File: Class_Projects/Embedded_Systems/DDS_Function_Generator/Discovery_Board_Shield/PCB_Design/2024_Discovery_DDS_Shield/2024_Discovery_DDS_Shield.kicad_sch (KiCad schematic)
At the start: 66 parts, among them J1 FILTER_CONN, J2 10118194-0001LF, J3 FTDI_UART_CONN, J4 DC_OFFSET_CONN, J5 LCD_CONN, J6 Conn_OpAmp_Power, J7 Conn_DiscBoard_Right, J8 Conn_DiscBoard_Left, J9 BNC_CONN, SW2 SW_MODE, SW3 SW_CURSOR, SW4 SW_PLUS, SW5 SW_MINUS, SW6 SW_RUN_STOP, U1 TL072, U2 TL072, U5 FT230XS

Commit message: new board version
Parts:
- removed J3: FTDI_UART_CONN, Connector_PinHeader_2.54mm:PinHeader_1x03_P2.54mm_Vertical, symbol Connector_Generic:Conn_01x03
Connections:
- net GND: no longer D3.1 (K), D4.1 (K)
- net MODE: now also R7.2, R8.2
- net at U5.14 (CBUS1): now also D3.1 (K); no longer R7.2
- net at U5.7 (CBUS2): now also D4.1 (K); no longer R8.2
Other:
- moved on the sheet: C17, C18, D3, D4, J2, R10, R7, R8, R9, SW2, SW3, SW4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

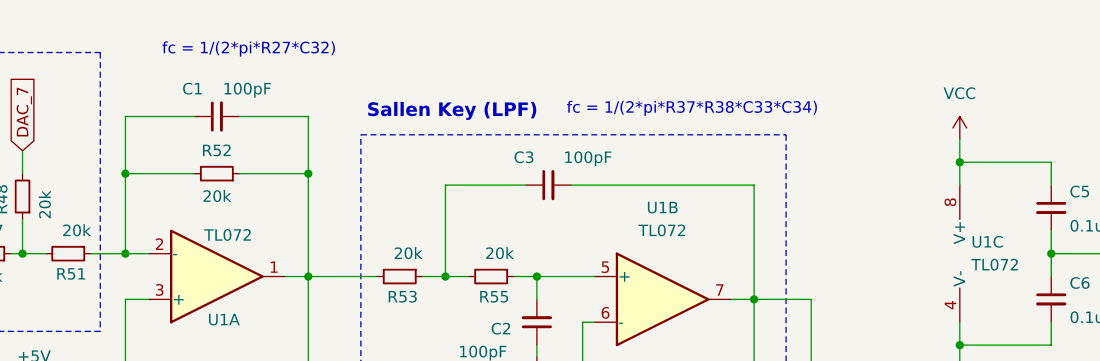
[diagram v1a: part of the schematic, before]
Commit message: schematics fixed
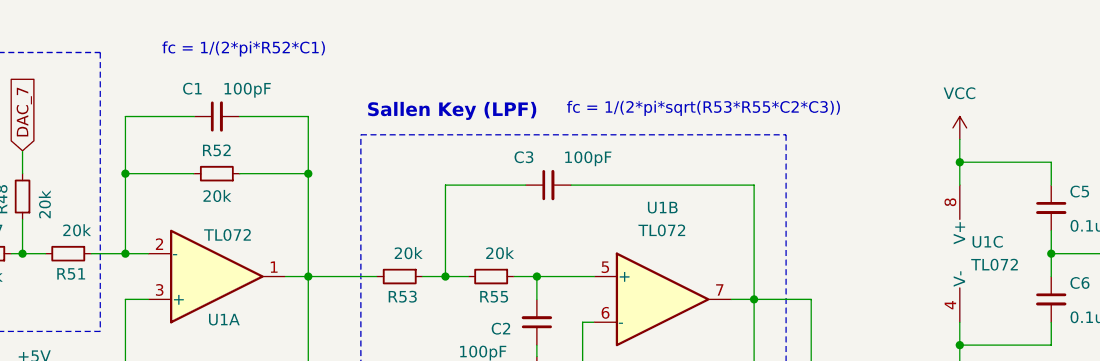
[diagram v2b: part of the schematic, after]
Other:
- note added: "fc = 1/(2*pi*R52*C1)"
- note added: "fc = 1/(2*pi*sqrt(R53*R55*C2*C3))"
- note removed: "fc = 1/(2*pi*R27*C32)"
- note removed: "fc = 1/(2*pi*R37*R38*C33*C34)"
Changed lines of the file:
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@@
 		)
 	)
-	(text "fc = 1/(2*pi*R37*R38*C33*C34)"
+	(text "fc = 1/(2*pi*sqrt(R53*R55*C2*C3))"
 		(exclude_from_sim no)
 		(at 154.432 25.908 0)
@@
 		)
 	)
-	(text "fc = 1/(2*pi*R27*C32)"
+	(text "fc = 1/(2*pi*R52*C1)"
 		(exclude_from_sim no)
 		(at 109.474 19.304 0)
